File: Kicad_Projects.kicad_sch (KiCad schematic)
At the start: 30 parts, among them J1 Ent. 15Vca, J2 Sal. Vcc Voltimetro/Amperimet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, J3 Sal. Tension regulable, J4 Sal. Amperimetro, Q1 BD137, Q2 TIP3055G, U1 LM723_DIP14

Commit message: Mejoras en PCB
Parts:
- R5: value 820 -> 1200
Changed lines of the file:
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@@
     (in_bom yes) (on_board yes) (fields_autoplaced)
     (property "Reference" "R5" (id 0) (at 161.29 110.49 90))
-    (property "Value" "820" (id 1) (at 161.29 113.03 90))
+    (property "Value" "1200" (id 1) (at 161.29 113.03 90))
     (property "Footprint" "Resistor_THT:R_Axial_DIN0207_L6.3mm_D2.5mm_P10.16mm_Horizontal" (id 2) (at 161.29 118.618 90)
       (effects (font (size 1.27 1.27)) hide)
@@
     )
     (path "/22d2f5d1-4df5-461f-991d-c8748c700a3d"
-      (reference "R5") (unit 1) (value "820") (footprint "Resistor_THT:R_Axial_DIN0207_L6.3mm_D2.5mm_P10.16mm_Horizontal")
+      (reference "R5") (unit 1) (value "1200") (footprint "Resistor_THT:R_Axial_DIN0207_L6.3mm_D2.5mm_P10.16mm_Horizontal")
     )
     (path "/f4a210db-a764-4c51-92ec-33db5d37f45b"

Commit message: Mejoras en PCB
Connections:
- net Vout_amp: now reaches J3.2 (Pin_2), J4.1 (Pin_1)
- net Vout: now reaches C6.1, C7.1, D7.1 (K), J3.1 (Pin_1), R3.1, RV2.2, RV2.3, U1.3 (CSEN)
- net TBJ_Out: now reaches D6.2 (A), D7.2 (A), Q2.3 (E), RV1.3
- net AC_F: now reaches D1.2 (A), D4.1 (K), J1.2 (Pin_2)
- net AC_N: now reaches D2.2 (A), D3.1 (K), J1.1 (Pin_1)
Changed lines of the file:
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@@
     (stroke (width 0) (type default) (color 0 0 0 0))
+  )
+  (global_label "Vout_amp" (shape input) (at 212.09 125.73 0) (fields_autoplaced)
+    (effects (font (size 1.27 1.27)) (justify left))
+    (property "Intersheet References" "${INTERSHEET_REFS}" (id 0) (at 223.5745 125.6506 0)
+      (effects (font (size 1.27 1.27)) (justify left) hide)
+    )
+  )
+  (global_label "Vout" (shape input) (at 191.77 107.95 0) (fields_autoplaced)
+    (effects (font (size 1.27 1.27)) (justify left))
+    (property "Intersheet References" "${INTERSHEET_REFS}" (id 0) (at 198.2955 107.8706 0)
+      (effects (font (size 1.27 1.27)) (justify left) hide)
+    )
+  )
+  (global_label "TBJ_Out" (shape input) (at 191.77 78.74 0) (fields_autoplaced)
+    (effects (font (size 1.27 1.27)) (justify left))
+    (property "Intersheet References" "${INTERSHEET_REFS}" (id 0) (at 201.5612 78.6606 0)
+      (effects (font (size 1.27 1.27)) (justify left) hide)
+    )
+  )
+  (global_label "AC_N" (shape input) (at 50.8 83.82 0) (fields_autoplaced)
+    (effects (font (size 1.27 1.27)) (justify left))
+    (property "Intersheet References" "${INTERSHEET_REFS}" (id 0) (at 57.8698 83.7406 0)
+      (effects (font (size 1.27 1.27)) (justify left) hide)
+    )
+  )
+  (global_label "AC_F" (shape input) (at 50.8 78.74 0) (fields_autoplaced)
+    (effects (font (size 1.27 1.27)) (justify left))
+    (property "Intersheet References" "${INTERSHEET_REFS}" (id 0) (at 57.6279 78.6606 0)
+      (effects (font (size 1.27 1.27)) (justify left) hide)
+    )
   )
   (symbol (lib_id "Connector_Generic:Conn_01x02") (at 125.73 66.04 90) (unit 1)

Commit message: Agregado de jumper
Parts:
- J2: value Sal. Vcc Voltimetro/Amperimetro -> Vcc_Volt/Amper
- J3: value Sal. Tension regulable -> Vout
- J4: value Sal. Amperimetro -> Amperimetro
- Regulacion_Tension1: renamed from 10k1; value R_Potentiometer -> 10k
- renumbered RV2 to Ajuste_Iout_max1, RV1 to Regulacion_Corriente1
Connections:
- net +VDC: now also J2.2 (Pin_2); no longer J2.1 (Pin_1)
- net GND: now also J2.1 (Pin_1); no longer J2.2 (Pin_2)
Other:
- moved on the sheet: J2
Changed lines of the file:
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@@
+    (stroke (width 0) (type default) (color 0 0 0 0))
+  )
+  (wire (pts (xy 125.73 72.39) (xy 125.73 78.74))
     (stroke (width 0) (type default) (color 0 0 0 0))
   )
@@
     (stroke (width 0) (type default) (color 0 0 0 0))
   )
-  (wire (pts (xy 128.27 71.12) (xy 128.27 73.66))
-    (stroke (width 0) (type default) (color 0 0 0 0))
-  )
   (wire (pts (xy 152.4 104.14) (xy 152.4 99.06))
     (stroke (width 0) (type default) (color 0 0 0 0))
@@
     (stroke (width 0) (type default) (color 0 0 0 0))
   )
-  (wire (pts (xy 125.73 71.12) (xy 125.73 78.74))
-    (stroke (width 0) (type default) (color 0 0 0 0))
-  )
   (wire (pts (xy 118.11 78.74) (xy 125.73 78.74))
     (stroke (width 0) (type default) (color 0 0 0 0))
@@
   )
   (wire (pts (xy 175.26 78.74) (xy 168.91 78.74))
+    (stroke (width 0) (type default) (color 0 0 0 0))
+  )
+  (wire (pts (xy 123.19 72.39) (xy 123.19 74.93))
     (stroke (width 0) (type default) (color 0 0 0 0))
   )
@@
     )
   )
-  (symbol (lib_id "Connector_Generic:Conn_01x02") (at 125.73 66.04 90) (unit 1)
-    (in_bom yes) (on_board yes) (fields_autoplaced)
-    (property "Reference" "J2" (id 0) (at 125.7299 63.5 0)
-      (effects (font (size 1.27 1.27)) (justify left))
-    )
-    (property "Value" "Sal. Vcc Voltimetro/Amperimetro" (id 1) (at 128.2699 63.5 0)
-      (effects (font (size 1.27 1.27)) (justify left))
-    )
-    (property "Footprint" "TerminalBlock:TerminalBlock_bornier-2_P5.08mm" (id 2) (at 125.73 66.04 0)
-      (effects (font (size 1.27 1.27)) hide)
-    )
-    (property "Datasheet" "~" (id 3) (at 125.73 66.04 0)
+  (symbol (lib_id "Connector_Generic:Conn_01x02") (at 123.19 67.31 90) (unit 1)
+    (in_bom yes) (on_board yes) (fields_autoplaced)
+    (property "Reference" "J2" (id 0) (at 128.27 66.0399 90)
+      (effects (font (size 1.27 1.27)) (justify right))
+    )
+    (property "Value" "Vcc_Volt/Amper" (id 1) (at 128.27 68.5799 90)
+      (effects (font (size 1.27 1.27)) (justify right))
+    )
+    (property "Footprint" "TerminalBlock:TerminalBlock_bornier-2_P5.08mm" (id 2) (at 123.19 67.31 0)
+      (effects (font (size 1.27 1.27)) hide)
+    )
+    (property "Datasheet" "~" (id 3) (at 123.19 67.31 0)
       (effects (font (size 1.27 1.27)) hide)
     )
@@
       (effects (font (size 1.27 1.27)) (justify left))
     )
-    (property "Value" "Sal. Amperimetro" (id 1) (at 220.98 132.0799 0)
+    (property "Value" "Amperimetro" (id 1) (at 220.98 132.0799 0)
       (effects (font (size 1.27 1.27)) (justify left))
     )
@@
       (effects (font (size 1.27 1.27)) (justify left))
     )
-    (property "Value" "Sal. Tension regulable" (id 1) (at 220.98 119.3799 0)
+    (property "Value" "Vout" (id 1) (at 220.98 119.3799 0)
       (effects (font (size 1.27 1.27)) (justify left))
     )
@@
     (pin "2")
   )
-  (symbol (lib_id "power:GND") (at 128.27 73.66 0) (unit 1)
-    (in_bom yes) (on_board yes) (fields_autoplaced)
-    (property "Reference" "#PWR06" (id 0) (at 128.27 80.01 0)
-      (effects (font (size 1.27 1.27)) hide)
-    )
-    (property "Value" "GND" (id 1) (at 128.27 78.74 0))
-    (property "Footprint" "" (id 2) (at 128.27 73.66 0)
-      (effects (font (size 1.27 1.27)) hide)
-    )
-    (property "Datasheet" "" (id 3) (at 128.27 73.66 0)
+  (symbol (lib_id "power:GND") (at 123.19 74.93 0) (unit 1)
+    (in_bom yes) (on_board yes) (fields_autoplaced)
+    (property "Reference" "#PWR06" (id 0) (at 123.19 81.28 0)
+      (effects (font (size 1.27 1.27)) hide)
+    )
+    (property "Value" "GND" (id 1) (at 123.19 80.01 0))
+    (property "Footprint" "" (id 2) (at 123.19 74.93 0)
+      (effects (font (size 1.27 1.27)) hide)
+    )
+    (property "Datasheet" "" (id 3) (at 123.19 74.93 0)
       (effects (font (size 1.27 1.27)) hide)
     )
@@
   (symbol (lib_id "Device:R_Potentiometer") (at 106.68 120.65 0) (unit 1)
     (in_bom yes) (on_board yes) (fields_autoplaced)
-    (property "Reference" "10k1" (id 0) (at 104.14 119.3799 0)
+    (property "Reference" "Regulacion_Tension1" (id 0) (at 104.14 119.3799 0)
       (effects (font (size 1.27 1.27)) (justify right))
     )
-    (property "Value" "R_Potentiometer" (id 1) (at 104.14 121.9199 0)
+    (property "Value" "10k" (id 1) (at 104.14 121.9199 0)
       (effects (font (size 1.27 1.27)) (justify right))
     )
@@
   (symbol (lib_id "Device:R_Potentiometer_Trim") (at 172.72 116.84 90) (unit 1)
     (in_bom yes) (on_board yes) (fields_autoplaced)
-    (property "Reference" "RV2" (id 0) (at 172.72 120.65 90))
+    (property "Reference" "Ajuste_Iout_max1" (id 0) (at 172.72 120.65 90))
     (property "Value" "500" (id 1) (at 172.72 123.19 90))
     (property "Footprint" "Potentiometer_THT:Potentiometer_Bourns_3266Y_Vertical" (id 2) (at 172.72 116.84 0)
@@
   (symbol (lib_id "Device:R_Potentiometer") (at 152.4 107.95 180) (unit 1)
     (in_bom yes) (on_board yes) (fields_autoplaced)
-    (property "Reference" "RV1" (id 0) (at 154.94 106.6799 0)
+    (property "Reference" "Regulacion_Corriente1" (id 0) (at 154.94 106.6799 0)
       (effects (font (size 1.27 1.27)) (justify right))
     )
@@
       (reference "#PWR0101") (unit 1) (value "+VDC") (footprint "")
     )
-    (path "/7c882e3d-ee53-4029-9e57-5934df1e910d"
-      (reference "10k1") (unit 1) (value "R_Potentiometer") (footprint "Potentiometer_THT:Potentiometer_ACP_CA9-H2,5_Horizontal")
+    (path "/b02653af-0c80-4cf8-a5b1-360f97e6ec36"
+      (reference "Ajuste_Iout_max1") (unit 1) (value "500") (footprint "Potentiometer_THT:Potentiometer_Bourns_3266Y_Vertical")
     )
     (path "/36d272cc-ceba-452e-8c80-67a18982be3a"
@@
     )
     (path "/0283546e-997b-4930-a208-94f7041523d6"
-      (reference "J2") (unit 1) (value "Sal. Vcc Voltimetro/Amperimetro") (footprint "TerminalBlock:TerminalBlock_bornier-2_P5.08mm")
+      (reference "J2") (unit 1) (value "Vcc_Volt/Amper") (footprint "TerminalBlock:TerminalBlock_bornier-2_P5.08mm")
     )
     (path "/0c266d60-30bc-4bff-8432-ac39bcdf57ef"
-      (reference "J3") (unit 1) (value "Sal. Tension regulable") (footprint "TerminalBlock:TerminalBlock_bornier-2_P5.08mm")
+      (reference "J3") (unit 1) (value "Vout") (footprint "TerminalBlock:TerminalBlock_bornier-2_P5.08mm")
     )
     (path "/054fdb65-4f12-4a90-9844-6d9aba346d66"
-      (reference "J4") (unit 1) (value "Sal. Amperimetro") (footprint "TerminalBlock:TerminalBlock_bornier-2_P5.08mm")
+      (reference "J4") (unit 1) (value "Amperimetro") (footprint "TerminalBlock:TerminalBlock_bornier-2_P5.08mm")
     )
     (path "/741aaae1-2444-44f5-aab9-533e74a65509"
@@
     )
     (path "/f4a210db-a764-4c51-92ec-33db5d37f45b"
-      (reference "RV1") (unit 1) (value "500") (footprint "Potentiometer_THT:Potentiometer_ACP_CA9-H2,5_Horizontal")
-    )
-    (path "/b02653af-0c80-4cf8-a5b1-360f97e6ec36"
-      (reference "RV2") (unit 1) (value "500") (footprint "Potentiometer_THT:Potentiometer_Bourns_3266Y_Vertical")
+      (reference "Regulacion_Corriente1") (unit 1) (value "500") (footprint "Potentiometer_THT:Potentiometer_ACP_CA9-H2,5_Horizontal")
+    )
+    (path "/7c882e3d-ee53-4029-9e57-5934df1e910d"
+      (reference "Regulacion_Tension1") (unit 1) (value "10k") (footprint "Potentiometer_THT:Potentiometer_ACP_CA9-H2,5_Horizontal")
     )
     (path "/7637b65c-9a41-4645-9c2e-9be3d6edf26b"

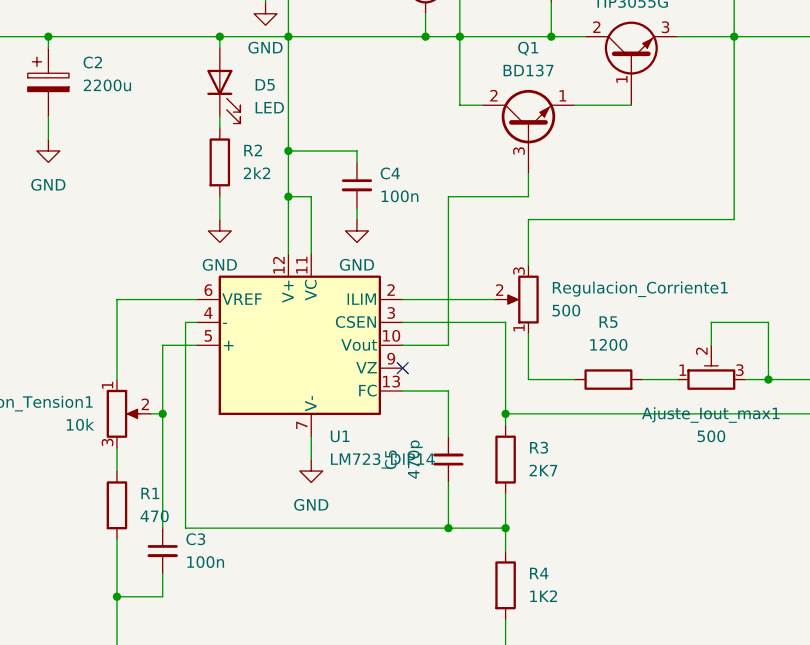
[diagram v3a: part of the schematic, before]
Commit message: cambio jumper y BOM en .csv
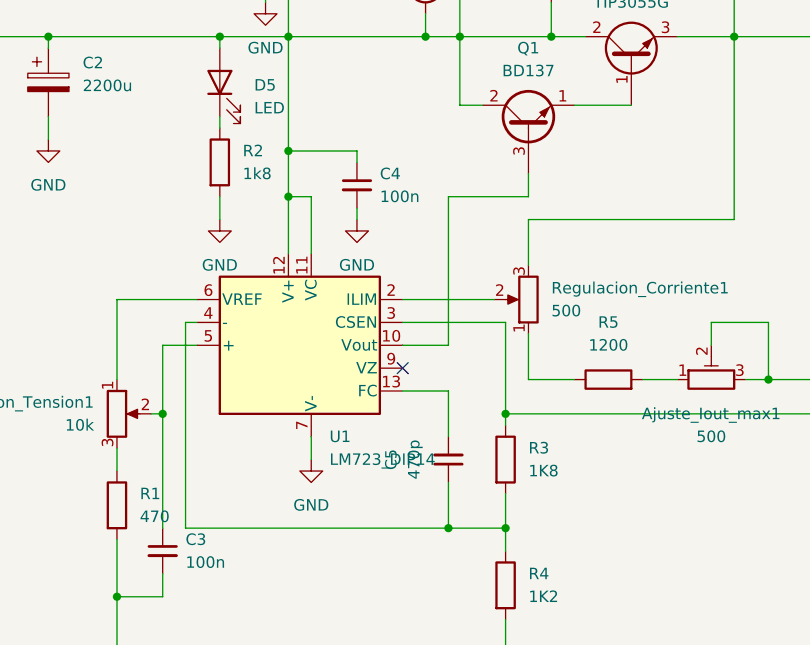
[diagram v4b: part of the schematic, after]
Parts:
- R2: value 2k2 -> 1k8
- R3: value 2K7 -> 1K8
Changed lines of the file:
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@@
       (effects (font (size 1.27 1.27)) (justify left))
     )
-    (property "Value" "2K7" (id 1) (at 152.4 126.9999 0)
+    (property "Value" "1K8" (id 1) (at 152.4 126.9999 0)
       (effects (font (size 1.27 1.27)) (justify left))
     )
@@
       (effects (font (size 1.27 1.27)) (justify left))
     )
-    (property "Value" "2k2" (id 1) (at 120.65 93.9799 0)
+    (property "Value" "1k8" (id 1) (at 120.65 93.9799 0)
       (effects (font (size 1.27 1.27)) (justify left))
     )
@@
     )
     (path "/c0ec9cbf-1981-4b2b-863c-b3bceb5501a6"
-      (reference "R2") (unit 1) (value "2k2") (footprint "Resistor_THT:R_Axial_DIN0207_L6.3mm_D2.5mm_P10.16mm_Horizontal")
+      (reference "R2") (unit 1) (value "1k8") (footprint "Resistor_THT:R_Axial_DIN0207_L6.3mm_D2.5mm_P10.16mm_Horizontal")
     )
     (path "/96684b02-cc18-45fd-af07-6ba5422caade"
-      (reference "R3") (unit 1) (value "2K7") (footprint "Resistor_THT:R_Axial_DIN0207_L6.3mm_D2.5mm_P10.16mm_Horizontal")
+      (reference "R3") (unit 1) (value "1K8") (footprint "Resistor_THT:R_Axial_DIN0207_L6.3mm_D2.5mm_P10.16mm_Horizontal")
     )
     (path "/a114a11f-bfc4-4928-86c4-97c65a6ed20e"

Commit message: Actualizacion Jumper 01/06
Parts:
- added JUMPER1: (no value), symbol Jumper:Jumper_2_Bridged
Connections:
- net Vout: now also JUMPER1.1 (A); no longer U1.3 (CSEN)
- new net: JUMPER1.2 (B), U1.3 (CSEN)
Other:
- moved on the sheet: R3
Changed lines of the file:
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@@
   (junction (at 106.68 140.97) (diameter 0) (color 0 0 0 0)
   )
-  (junction (at 191.77 120.65) (diameter 0) (color 0 0 0 0)
+  (junction (at 149.86 121.92) (diameter 0) (color 0 0 0 0)
   )
   (junction (at 125.73 96.52) (diameter 0) (color 0 0 0 0)
@@
   (junction (at 55.88 85.09) (diameter 0) (color 0 0 0 0)
   )
-  (junction (at 149.86 120.65) (diameter 0) (color 0 0 0 0)
-  )
   (junction (at 99.06 78.74) (diameter 0) (color 0 0 0 0)
   )
@@
   )
   (junction (at 125.73 78.74) (diameter 0) (color 0 0 0 0)
+  )
+  (junction (at 191.77 121.92) (diameter 0) (color 0 0 0 0)
   )
   (junction (at 191.77 116.84) (diameter 0) (color 0 0 0 0)
@@
     (stroke (width 0) (type default) (color 0 0 0 0))
   )
+  (wire (pts (xy 149.86 121.92) (xy 191.77 121.92))
+    (stroke (width 0) (type default) (color 0 0 0 0))
+  )
   (wire (pts (xy 154.94 74.93) (xy 154.94 78.74))
     (stroke (width 0) (type default) (color 0 0 0 0))
@@
     (stroke (width 0) (type default) (color 0 0 0 0))
   )
-  (wire (pts (xy 149.86 110.49) (xy 149.86 120.65))
-    (stroke (width 0) (type default) (color 0 0 0 0))
-  )
   (wire (pts (xy 198.12 116.84) (xy 191.77 116.84))
     (stroke (width 0) (type default) (color 0 0 0 0))
@@
     (stroke (width 0) (type default) (color 0 0 0 0))
   )
-  (wire (pts (xy 191.77 120.65) (xy 191.77 116.84))
+  (wire (pts (xy 191.77 116.84) (xy 191.77 121.92))
     (stroke (width 0) (type default) (color 0 0 0 0))
   )
@@
     (stroke (width 0) (type default) (color 0 0 0 0))
   )
+  (wire (pts (xy 191.77 121.92) (xy 191.77 132.08))
+    (stroke (width 0) (type default) (color 0 0 0 0))
+  )
   (wire (pts (xy 125.73 91.44) (xy 125.73 96.52))
     (stroke (width 0) (type default) (color 0 0 0 0))
@@
     (stroke (width 0) (type default) (color 0 0 0 0))
   )
+  (wire (pts (xy 149.86 120.65) (xy 149.86 121.92))
+    (stroke (width 0) (type default) (color 0 0 0 0))
+  )
   (wire (pts (xy 125.73 78.74) (xy 140.97 78.74))
     (stroke (width 0) (type default) (color 0 0 0 0))
@@
     (stroke (width 0) (type default) (color 0 0 0 0))
   )
-  (wire (pts (xy 149.86 120.65) (xy 191.77 120.65))
-    (stroke (width 0) (type default) (color 0 0 0 0))
-  )
   (wire (pts (xy 138.43 107.95) (xy 148.59 107.95))
     (stroke (width 0) (type default) (color 0 0 0 0))
   )
-  (wire (pts (xy 191.77 132.08) (xy 191.77 120.65))
-    (stroke (width 0) (type default) (color 0 0 0 0))
-  )
   (wire (pts (xy 157.48 86.36) (xy 163.83 86.36))
     (stroke (width 0) (type default) (color 0 0 0 0))
@@
     (stroke (width 0) (type default) (color 0 0 0 0))
   )
-  (wire (pts (xy 149.86 120.65) (xy 149.86 121.92))
-    (stroke (width 0) (type default) (color 0 0 0 0))
-  )
   (wire (pts (xy 59.69 78.74) (xy 53.34 78.74))
     (stroke (width 0) (type default) (color 0 0 0 0))
@@
     (stroke (width 0) (type default) (color 0 0 0 0))
   )
-  (wire (pts (xy 149.86 129.54) (xy 149.86 133.35))
+  (wire (pts (xy 149.86 130.81) (xy 149.86 133.35))
     (stroke (width 0) (type default) (color 0 0 0 0))
   )
@@
   )
   (wire (pts (xy 175.26 78.74) (xy 168.91 78.74))
+    (stroke (width 0) (type default) (color 0 0 0 0))
+  )
+  (wire (pts (xy 149.86 121.92) (xy 149.86 123.19))
     (stroke (width 0) (type default) (color 0 0 0 0))
   )
@@
     (pin "1")
   )
-  (symbol (lib_id "Device:R") (at 149.86 125.73 0) (unit 1)
-    (in_bom yes) (on_board yes) (fields_autoplaced)
-    (property "Reference" "R3" (id 0) (at 152.4 124.4599 0)
-      (effects (font (size 1.27 1.27)) (justify left))
-    )
-    (property "Value" "1K8" (id 1) (at 152.4 126.9999 0)
-      (effects (font (size 1.27 1.27)) (justify left))
-    )
-    (property "Footprint" "Resistor_THT:R_Axial_DIN0207_L6.3mm_D2.5mm_P10.16mm_Horizontal" (id 2) (at 148.082 125.73 90)
-      (effects (font (size 1.27 1.27)) hide)
-    )
-    (property "Datasheet" "~" (id 3) (at 149.86 125.73 0)
+  (symbol (lib_id "Device:R") (at 149.86 127 0) (unit 1)
+    (in_bom yes) (on_board yes) (fields_autoplaced)
+    (property "Reference" "R3" (id 0) (at 152.4 125.7299 0)
+      (effects (font (size 1.27 1.27)) (justify left))
+    )
+    (property "Value" "1K8" (id 1) (at 152.4 128.2699 0)
+      (effects (font (size 1.27 1.27)) (justify left))
+    )
+    (property "Footprint" "Resistor_THT:R_Axial_DIN0207_L6.3mm_D2.5mm_P10.16mm_Horizontal" (id 2) (at 148.082 127 90)
+      (effects (font (size 1.27 1.27)) hide)
+    )
+    (property "Datasheet" "~" (id 3) (at 149.86 127 0)
       (effects (font (size 1.27 1.27)) hide)
     )
@@
   )
   (symbol (lib_id "Device:R_Potentiometer_Trim") (at 172.72 116.84 90) (unit 1)
-    (in_bom yes) (on_board yes) (fields_autoplaced)
-    (property "Reference" "Ajuste_Iout_max1" (id 0) (at 172.72 120.65 90))
-    (property "Value" "500" (id 1) (at 172.72 123.19 90))
+    (in_bom yes) (on_board yes)
+    (property "Reference" "Ajuste_Iout_max1" (id 0) (at 176.53 109.22 90))
+    (property "Value" "500" (id 1) (at 172.72 119.38 90))
     (property "Footprint" "Potentiometer_THT:Potentiometer_Bourns_3266Y_Vertical" (id 2) (at 172.72 116.84 0)
       (effects (font (size 1.27 1.27)) hide)
@@
     (pin "1")
   )
+  (symbol (lib_id "Jumper:Jumper_2_Bridged") (at 149.86 115.57 90) (unit 1)
+    (in_bom yes) (on_board yes)
+    (property "Reference" "JUMPER1" (id 0) (at 151.13 115.57 90)
+      (effects (font (size 1.27 1.27)) (justify right))
+    )
+    (property "Value" "" (id 1) (at 160.02 124.46 0)
+      (effects (font (size 1.27 1.27)) (justify right))
+    )
+    (property "Footprint" "" (id 2) (at 149.86 115.57 0)
+      (effects (font (size 1.27 1.27)) hide)
+    )
+    (property "Datasheet" "~" (id 3) (at 149.86 115.57 0)
+      (effects (font (size 1.27 1.27)) hide)
+    )
+    (pin "1")
+    (pin "2")
+  )
   (symbol (lib_id "Device:C_Polarized") (at 99.06 83.82 0) (unit 1)
     (in_bom yes) (on_board yes) (fields_autoplaced)
@@
       (reference "J4") (unit 1) (value "Amperimetro") (footprint "TerminalBlock:TerminalBlock_bornier-2_P5.08mm")
     )
+    (path "/dff5dc14-121e-4820-8bdd-194a2b3cb201"
+      (reference "JUMPER1") (unit 1) (value "Jumper_2_Bridged") (footprint "Resistor_THT:R_Axial_DIN0207_L6.3mm_D2.5mm_P10.16mm_Horizontal")
+    )
     (path "/741aaae1-2444-44f5-aab9-533e74a65509"
